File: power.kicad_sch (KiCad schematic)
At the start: 29 parts, among them J3 Conn_01x03_Male, Q1 DMP1045U-7, Q2 UMW8205A, U2 TP4056M, U3 DW01A-G

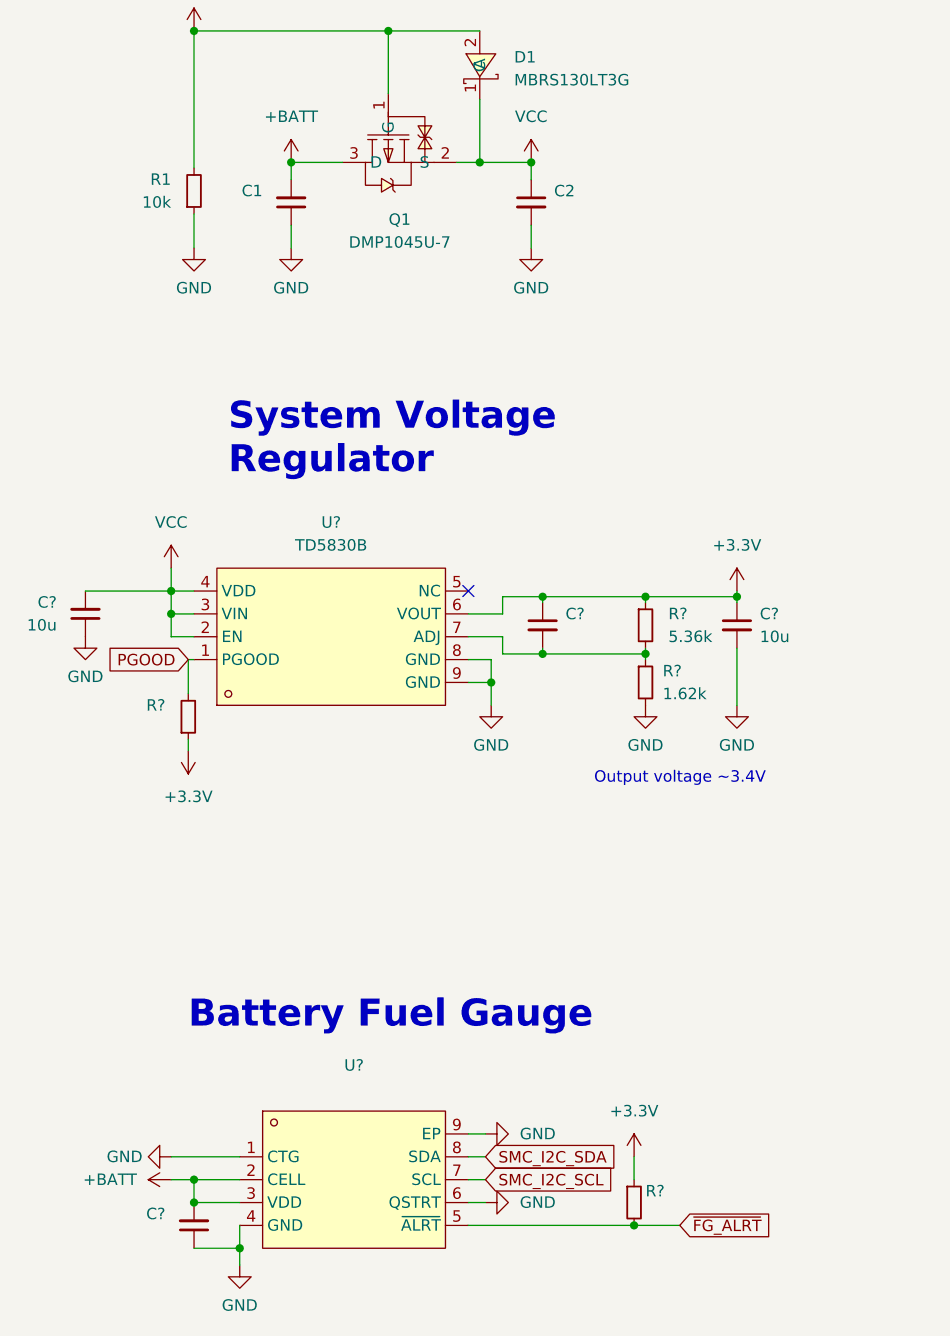
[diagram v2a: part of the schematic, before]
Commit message: schem: first pass done, ERC passing
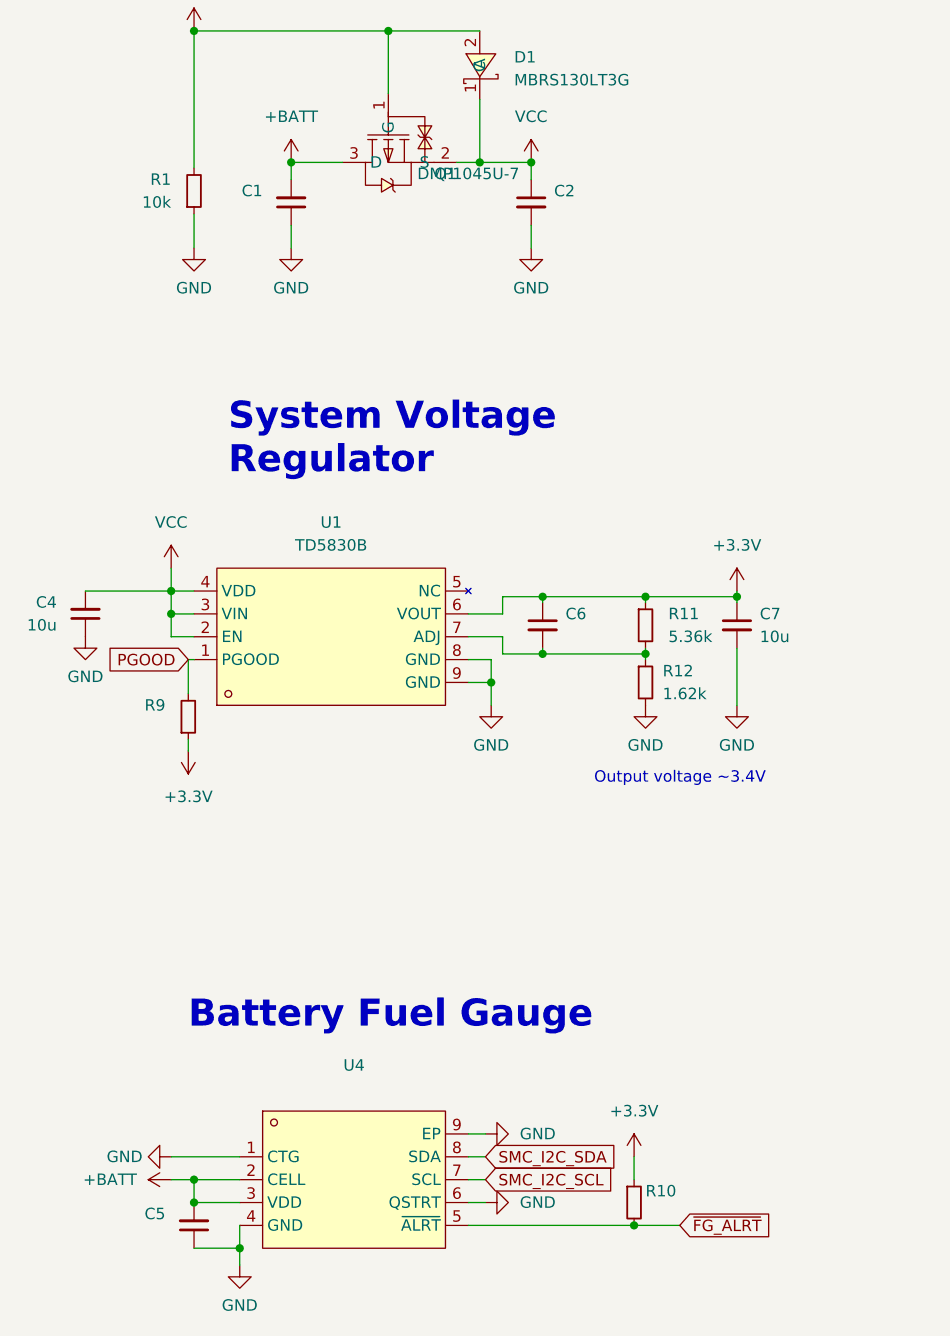
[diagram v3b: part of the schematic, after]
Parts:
- U4: renamed from U?; footprint (none) -> lcsc:DFN-8_L2.0-W2.0-P0.50-BL-EP
- gave numbers to parts that had none: 9
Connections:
- no-connect marks 3 -> 2
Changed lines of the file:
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@@
   (junction (at 42.545 94.615) (diameter 0) (color 0 0 0 0)
   )
-  (no_connect (at 75.565 94.615))
+  (no_connect (at 224.155 88.265))
   (no_connect (at 250.825 67.945))
-  (no_connect (at 224.155 88.265))
   (wire (pts (xy 248.285 134.62) (xy 248.285 132.715))
     (stroke (width 0) (type default) (color 0 0 0 0))
@@
   (symbol (lib_id "power:GND") (at 95.25 107.315 0) (unit 1)
     (in_bom yes) (on_board yes) (fields_autoplaced)
-    (property "Reference" "#PWR?" (id 0) (at 95.25 113.665 0)
+    (property "Reference" "#PWR031" (id 0) (at 95.25 113.665 0)
       (effects (font (size 1.27 1.27)) hide)
     )
@@
   (symbol (lib_id "Device:C_Small") (at 33.02 97.155 0) (mirror x) (unit 1)
     (in_bom yes) (on_board yes) (fields_autoplaced)
-    (property "Reference" "C?" (id 0) (at 29.845 95.8785 0)
+    (property "Reference" "C4" (id 0) (at 29.845 95.8785 0)
       (effects (font (size 1.27 1.27)) (justify right))
     )
@@
   (symbol (lib_id "power:+3.3V") (at 44.45 112.395 180) (unit 1)
     (in_bom yes) (on_board yes) (fields_autoplaced)
-    (property "Reference" "#PWR?" (id 0) (at 44.45 108.585 0)
+    (property "Reference" "#PWR025" (id 0) (at 44.45 108.585 0)
       (effects (font (size 1.27 1.27)) hide)
     )
@@
   (symbol (lib_id "Device:C_Small") (at 105.41 98.425 0) (unit 1)
     (in_bom yes) (on_board yes) (fields_autoplaced)
-    (property "Reference" "C?" (id 0) (at 107.95 97.1612 0)
+    (property "Reference" "C7" (id 0) (at 107.95 97.1612 0)
       (effects (font (size 1.27 1.27)) (justify left))
     )
@@
   (symbol (lib_id "power:GND") (at 77.47 162.56 90) (unit 1)
     (in_bom yes) (on_board yes) (fields_autoplaced)
-    (property "Reference" "#PWR?" (id 0) (at 83.82 162.56 0)
+    (property "Reference" "#PWR028" (id 0) (at 83.82 162.56 0)
       (effects (font (size 1.27 1.27)) hide)
     )
@@
   (symbol (lib_id "lcsc:TD5830B") (at 60.325 99.695 0) (mirror x) (unit 1)
     (in_bom yes) (on_board yes) (fields_autoplaced)
-    (property "Reference" "U?" (id 0) (at 60.325 86.995 0))
+    (property "Reference" "U1" (id 0) (at 60.325 86.995 0))
     (property "Value" "TD5830B" (id 1) (at 60.325 89.535 0))
     (property "Footprint" "lcsc:SOP-8_L4.9-W3.9-P1.27-LS6.0-BL-EP" (id 2) (at 60.325 86.995 0)
@@
   (symbol (lib_id "lcsc:DMP1045U-7") (at 66.675 46.99 90) (mirror x) (unit 1)
     (in_bom yes) (on_board yes) (fields_autoplaced)
-    (property "Reference" "Q1" (id 0) (at 67.945 53.34 90))
-    (property "Value" "DMP1045U-7" (id 1) (at 67.945 55.88 90))
-    (property "Footprint" "lcsc:SOT-23-3_L2.9-W1.3-P1.90-LS2.4-BR" (id 2) (at 81.915 46.99 0)
-      (effects (font (size 1.27 1.27)) hide)
-    )
-    (property "Datasheet" "https://lcsc.com/product-detail/Others_Diodes-Incorporated_DMP1045U-7_Diodes-Incorporated-DMP1045U-7_C177033.html" (id 3) (at 84.455 46.99 0)
-      (effects (font (size 1.27 1.27)) hide)
-    )
-    (property "Manufacturer" "Diodes Incorporated" (id 4) (at 86.995 46.99 0)
-      (effects (font (size 1.27 1.27)) hide)
-    )
-    (property "LCSC Part" "C177033" (id 5) (at 89.535 46.99 0)
-      (effects (font (size 1.27 1.27)) hide)
-    )
-    (property "JLC Part" "Extended Part" (id 6) (at 92.075 46.99 0)
+    (property "Reference" "Q1" (id 0) (at 73.025 48.26 90))
+    (property "Value" "DMP1045U-7" (id 1) (at 75.565 48.26 90))
+    (property "Footprint" "lcsc:SOT-23-3_L2.9-W1.3-P1.90-LS2.4-BR" (id 2) (at 66.675 62.23 0)
+      (effects (font (size 1.27 1.27)) hide)
+    )
+    (property "Datasheet" "https://lcsc.com/product-detail/Others_Diodes-Incorporated_DMP1045U-7_Diodes-Incorporated-DMP1045U-7_C177033.html" (id 3) (at 66.675 64.77 0)
+      (effects (font (size 1.27 1.27)) hide)
+    )
+    (property "Manufacturer" "Diodes Incorporated" (id 4) (at 66.675 67.31 0)
+      (effects (font (size 1.27 1.27)) hide)
+    )
+    (property "LCSC Part" "C177033" (id 5) (at 66.675 69.85 0)
+      (effects (font (size 1.27 1.27)) hide)
+    )
+    (property "JLC Part" "Extended Part" (id 6) (at 66.675 72.39 0)
       (effects (font (size 1.27 1.27)) hide)
     )
@@
   (symbol (lib_id "power:GND") (at 42.545 157.48 270) (unit 1)
     (in_bom yes) (on_board yes) (fields_autoplaced)
-    (property "Reference" "#PWR?" (id 0) (at 36.195 157.48 0)
+    (property "Reference" "#PWR023" (id 0) (at 36.195 157.48 0)
       (effects (font (size 1.27 1.27)) hide)
     )
@@
   (symbol (lib_id "power:+3.3V") (at 93.98 157.48 0) (unit 1)
     (in_bom yes) (on_board yes) (fields_autoplaced)
-    (property "Reference" "#PWR?" (id 0) (at 93.98 161.29 0)
+    (property "Reference" "#PWR030" (id 0) (at 93.98 161.29 0)
       (effects (font (size 1.27 1.27)) hide)
     )
@@
   (symbol (lib_id "Device:R_Small") (at 44.45 108.585 0) (mirror x) (unit 1)
     (in_bom yes) (on_board yes) (fields_autoplaced)
-    (property "Reference" "R?" (id 0) (at 41.91 107.3149 0)
+    (property "Reference" "R9" (id 0) (at 41.91 107.3149 0)
       (effects (font (size 1.27 1.27)) (justify right))
     )
@@
   (symbol (lib_id "Device:R_Small") (at 93.98 162.56 0) (unit 1)
     (in_bom yes) (on_board yes)
-    (property "Reference" "R?" (id 0) (at 95.25 161.29 0)
+    (property "Reference" "R10" (id 0) (at 95.25 161.29 0)
       (effects (font (size 1.27 1.27)) (justify left))
     )
@@
   (symbol (lib_id "power:GND") (at 77.47 154.94 90) (unit 1)
     (in_bom yes) (on_board yes) (fields_autoplaced)
-    (property "Reference" "#PWR?" (id 0) (at 83.82 154.94 0)
+    (property "Reference" "#PWR027" (id 0) (at 83.82 154.94 0)
       (effects (font (size 1.27 1.27)) hide)
     )
@@
   (symbol (lib_id "Device:R_Small") (at 95.25 98.425 0) (unit 1)
     (in_bom yes) (on_board yes) (fields_autoplaced)
-    (property "Reference" "R?" (id 0) (at 97.79 97.1549 0)
+    (property "Reference" "R11" (id 0) (at 97.79 97.1549 0)
       (effects (font (size 1.27 1.27)) (justify left))
     )
@@
   (symbol (lib_id "power:+BATT") (at 42.545 160.02 90) (unit 1)
     (in_bom yes) (on_board yes) (fields_autoplaced)
-    (property "Reference" "#PWR?" (id 0) (at 46.355 160.02 0)
+    (property "Reference" "#PWR024" (id 0) (at 46.355 160.02 0)
       (effects (font (size 1.27 1.27)) hide)
     )
@@
   (symbol (lib_id "power:VCC") (at 42.545 92.075 0) (unit 1)
     (in_bom yes) (on_board yes) (fields_autoplaced)
-    (property "Reference" "#PWR?" (id 0) (at 42.545 95.885 0)
+    (property "Reference" "#PWR022" (id 0) (at 42.545 95.885 0)
       (effects (font (size 1.27 1.27)) hide)
     )
@@
   (symbol (lib_id "Device:C_Small") (at 83.82 98.425 0) (unit 1)
     (in_bom yes) (on_board yes) (fields_autoplaced)
-    (property "Reference" "C?" (id 0) (at 86.36 97.1612 0)
+    (property "Reference" "C6" (id 0) (at 86.36 97.1612 0)
       (effects (font (size 1.27 1.27)) (justify left))
     )
@@
   (symbol (lib_id "power:GND") (at 50.165 169.545 0) (unit 1)
     (in_bom yes) (on_board yes) (fields_autoplaced)
-    (property "Reference" "#PWR?" (id 0) (at 50.165 175.895 0)
+    (property "Reference" "#PWR026" (id 0) (at 50.165 175.895 0)
       (effects (font (size 1.27 1.27)) hide)
     )
@@
   (symbol (lib_id "power:+3.3V") (at 105.41 94.615 0) (unit 1)
     (in_bom yes) (on_board yes) (fields_autoplaced)
-    (property "Reference" "#PWR?" (id 0) (at 105.41 98.425 0)
+    (property "Reference" "#PWR032" (id 0) (at 105.41 98.425 0)
       (effects (font (size 1.27 1.27)) hide)
     )
@@
   (symbol (lib_id "Device:R_Small") (at 95.25 104.775 0) (unit 1)
     (in_bom yes) (on_board yes) (fields_autoplaced)
-    (property "Reference" "R?" (id 0) (at 97.155 103.5049 0)
+    (property "Reference" "R12" (id 0) (at 97.155 103.5049 0)
       (effects (font (size 1.27 1.27)) (justify left))
     )
@@
   (symbol (lib_id "power:GND") (at 33.02 99.695 0) (unit 1)
     (in_bom yes) (on_board yes) (fields_autoplaced)
-    (property "Reference" "#PWR?" (id 0) (at 33.02 106.045 0)
+    (property "Reference" "#PWR01" (id 0) (at 33.02 106.045 0)
       (effects (font (size 1.27 1.27)) hide)
     )
@@
   (symbol (lib_id "Device:C_Small") (at 45.085 165.1 0) (mirror x) (unit 1)
     (in_bom yes) (on_board yes) (fields_autoplaced)
-    (property "Reference" "C?" (id 0) (at 41.91 163.8235 0)
+    (property "Reference" "C5" (id 0) (at 41.91 163.8235 0)
       (effects (font (size 1.27 1.27)) (justify right))
     )
@@
   (symbol (lib_id "power:GND") (at 105.41 107.315 0) (unit 1)
     (in_bom yes) (on_board yes) (fields_autoplaced)
-    (property "Reference" "#PWR?" (id 0) (at 105.41 113.665 0)
+    (property "Reference" "#PWR033" (id 0) (at 105.41 113.665 0)
       (effects (font (size 1.27 1.27)) hide)
     )
@@
   (symbol (lib_id "lcsc:MAX17048G+T10") (at 62.865 160.02 0) (unit 1)
     (in_bom yes) (on_board yes) (fields_autoplaced)
-    (property "Reference" "U?" (id 0) (at 62.865 147.32 0))
+    (property "Reference" "U4" (id 0) (at 62.865 147.32 0))
     (property "Value" "" (id 1) (at 62.865 149.86 0))
-    (property "Footprint" "" (id 2) (at 62.865 172.72 0)
+    (property "Footprint" "lcsc:DFN-8_L2.0-W2.0-P0.50-BL-EP" (id 2) (at 62.865 172.72 0)
       (effects (font (size 1.27 1.27)) hide)
     )
@@
   (symbol (lib_id "power:GND") (at 78.105 107.315 0) (unit 1)
     (in_bom yes) (on_board yes) (fields_autoplaced)
-    (property "Reference" "#PWR?" (id 0) (at 78.105 113.665 0)
-      (effects (font (size 1.27 1.27)) hide)
-    )
+    (property "Reference" "#PWR029" (id 0) (at 78.105 113.665 0)
+      (effects (font (size 1.27 1.27)) hide)
+    )
